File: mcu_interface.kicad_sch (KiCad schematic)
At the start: 6 parts, among them U2 MSP430FR2355TPT, Y1 Crystal

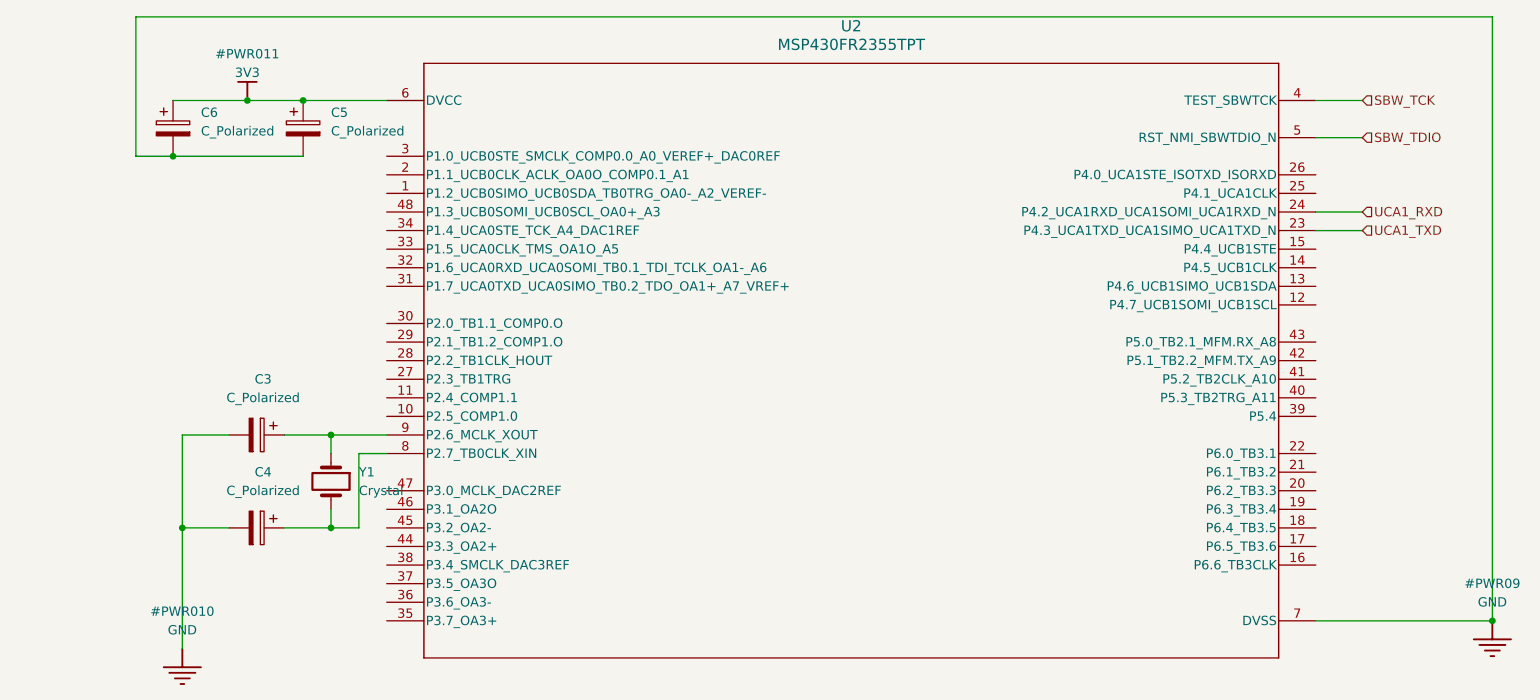
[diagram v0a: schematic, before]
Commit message: Updated Ports and Components in MCU Interface
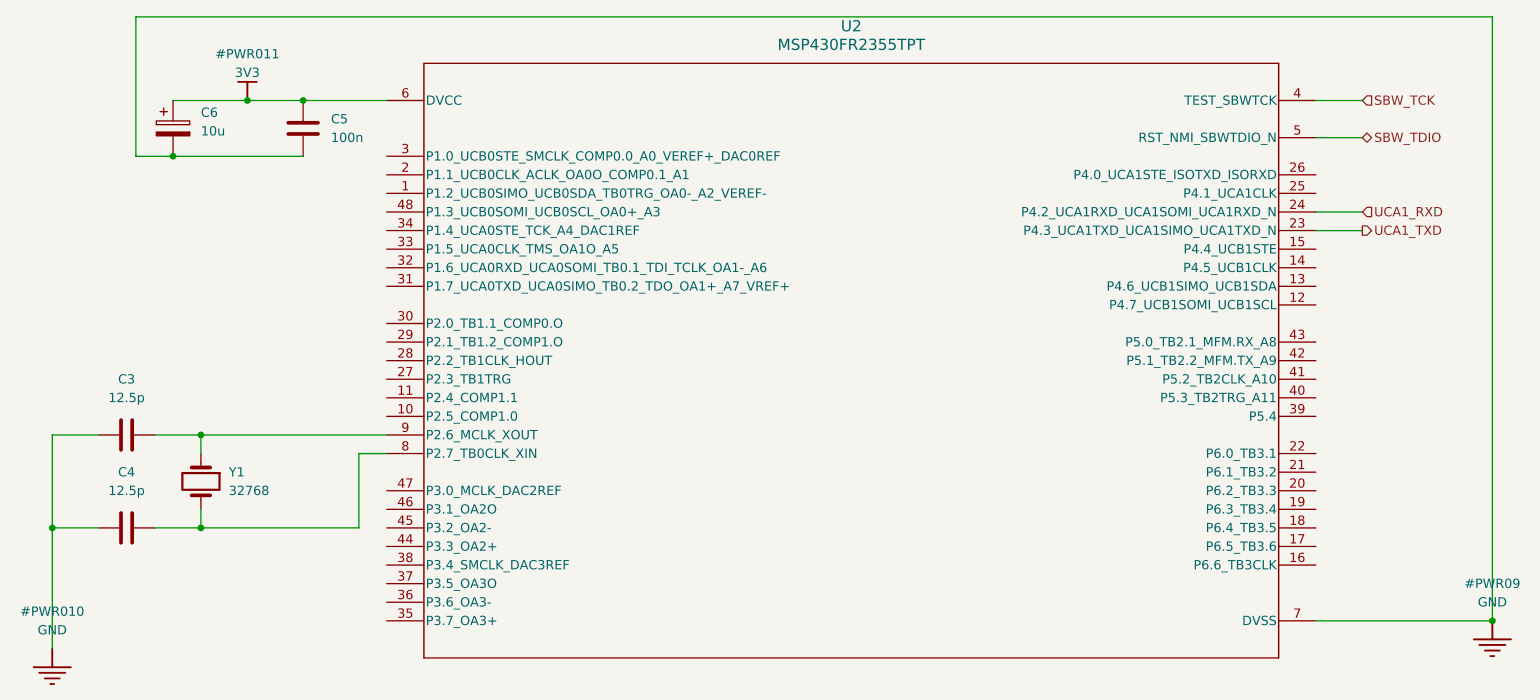
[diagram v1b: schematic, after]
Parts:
- removed C3, C4, C5: C_Polarized, symbol Device:C_Polarized
- added C3, C4: 12.5p, symbol Device:C
- added C5: 100n, symbol Device:C
- C6: value C_Polarized -> 10u
- Y1: value Crystal -> 32768; Part Number (none) -> MS3V-T1R-32.768kHz-12.5pF-20PPM-TA-QC-Au
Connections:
- net 3V3: now also C5.1
- net GND: now also C3.2, C4.2, C5.2
- net at U2.8 (P2.7_TB0CLK_XIN), Y1.2: now also C4.1
- net at U2.9 (P2.6_MCLK_XOUT), Y1.1: now also C3.1
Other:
- moved on the sheet: Y1
